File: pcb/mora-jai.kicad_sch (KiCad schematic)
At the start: 31 parts, among them J1 Conn_01x02, J2 Conn_01x04, J3 Conn_01x02, J4 Conn_01x02, J5 Conn_01x03, Q2 NPN, SW1 SW_Push, SW10 SW_Push, SW11 SW_Push, SW12 SW_Push, SW13 SW_Push, SW14 SW_Push, SW15 SW_Push, SW16 SW_Push, SW2 SW_Push, SW3 SW_Push, SW4 SW_Push, SW5 SW_Push, SW6 SW_Push, SW7 SW_Push, SW8 SW_Push, SW9 SW_Push, U1 CD74HC4067M, U3 XIAO-ESP32-S3-SMD

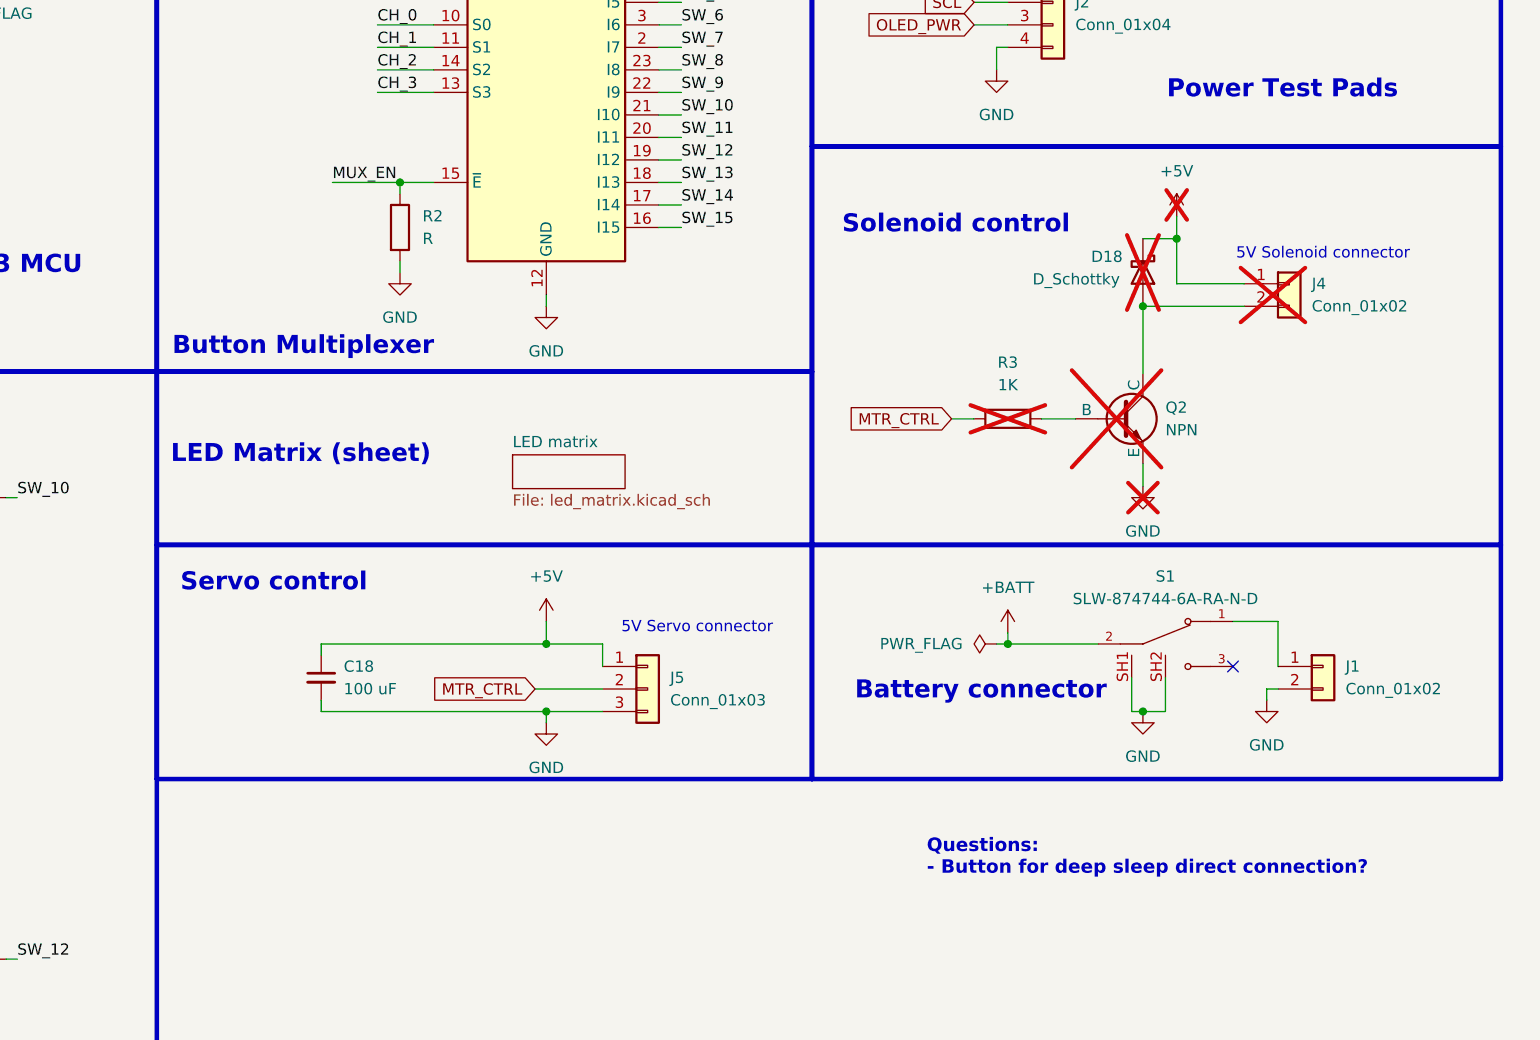
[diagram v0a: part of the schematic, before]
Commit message: remove solenoid control circuit, switching to servo
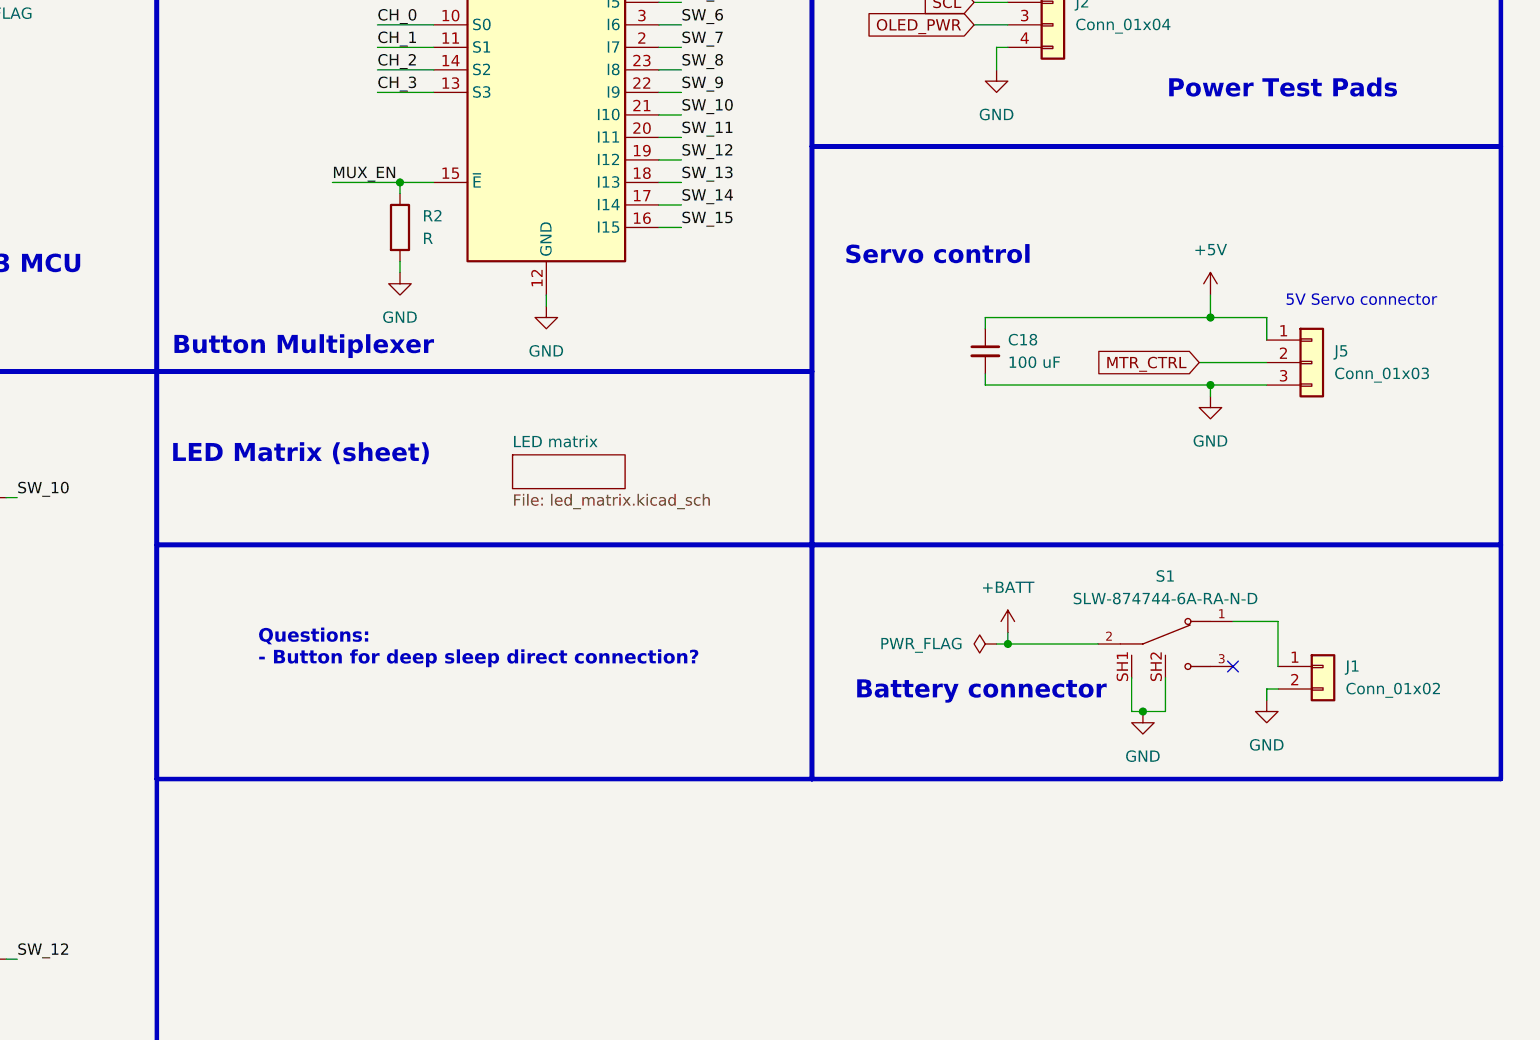
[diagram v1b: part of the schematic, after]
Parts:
- removed D18: D_Schottky, symbol Device:D_Schottky
- removed J4: Conn_01x02, Connector_JST:JST_PH_S2B-PH-K_1x02_P2.00mm_Horizontal, symbol Connector_Generic:Conn_01x02
- removed Q2: NPN, symbol Simulation_SPICE:NPN
- removed R3: 1K, symbol Device:R
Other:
- note removed: "5V Solenoid connector"
- note removed: "Solenoid control"
- moved on the sheet: C18, J5

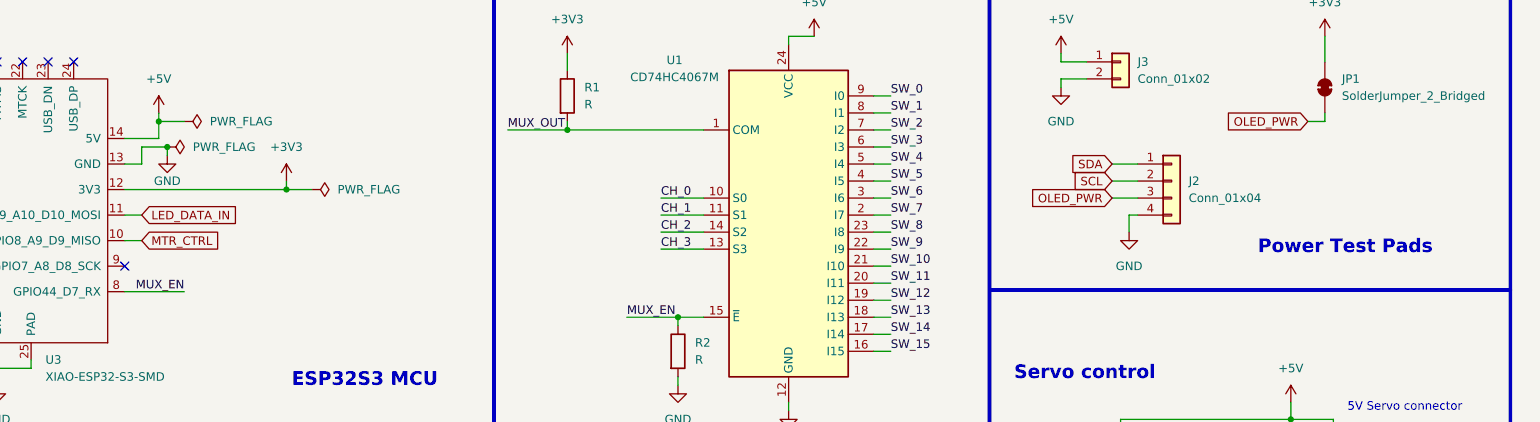
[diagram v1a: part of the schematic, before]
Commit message: positioning OLED
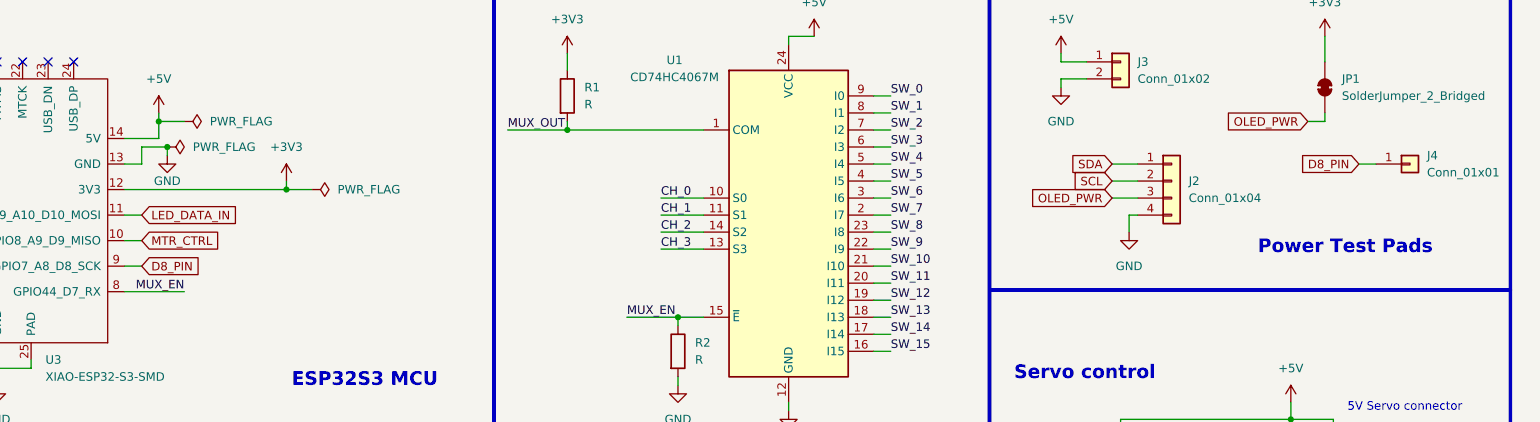
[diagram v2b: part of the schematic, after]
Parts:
- added J4: Conn_01x01, Connector_PinHeader_2.54mm:PinHeader_1x01_P2.54mm_Vertical, symbol Connector_Generic:Conn_01x01
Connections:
- net D8_PIN: now reaches U3.9 (GPIO7_A8_D8_SCK)
- net D8_PIN: now also J4.1 (Pin_1)
- no-connect marks 10 -> 9
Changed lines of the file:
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@@
 		(at 58.42 24.13)
 	)
-	(no_connect
-		(at 77.47 54.61)
-	)
 	(wire
 		(pts
@@
 	(wire
 		(pts
+			(xy 77.47 54.61) (xy 80.01 54.61)
+		)
+		(stroke
+			(width 0)
+			(type default)
+		)
+	)
+	(wire
+		(pts
 			(xy 87.63 143.51) (xy 87.63 139.7)
 		)
@@
 	(wire
 		(pts
+			(xy 261.62 39.37) (xy 264.16 39.37)
+		)
+		(stroke
+			(width 0)
+			(type default)
+		)
+	)
+	(wire
+		(pts
 			(xy 227.33 49.53) (xy 227.33 46.99)
 		)
@@
 		)
 	)
+	(global_label "D8_PIN"
+		(shape input)
+		(at 80.01 54.61 0)
+		(fields_autoplaced yes)
+		(effects
+			(font
+				(size 1.27 1.27)
+			)
+			(justify left)
+		)
+		(property "Intersheetrefs" "${INTERSHEET_REFS}"
+			(at 89.6476 54.61 0)
+			(hide yes)
+			(show_name no)
+			(do_not_autoplace no)
+			(effects
+				(font
+					(size 1.27 1.27)
+				)
+				(justify left)
+			)
+		)
+	)
+	(global_label "D8_PIN"
+		(shape input)
+		(at 261.62 39.37 180)
+		(fields_autoplaced yes)
+		(effects
+			(font
+				(size 1.27 1.27)
+			)
+			(justify right)
+		)
+		(property "Intersheetrefs" "${INTERSHEET_REFS}"
+			(at 251.9824 39.37 0)
+			(hide yes)
+			(show_name no)
+			(do_not_autoplace no)
+			(effects
+				(font
+					(size 1.27 1.27)
+				)
+				(justify right)
+			)
+		)
+	)
 	(global_label "LED_DATA_IN"
 		(shape input)
@@
 					(unit 1)
 				)
+			)
+		)
+	)
+	(symbol
+		(lib_id "Connector_Generic:Conn_01x01")
+		(at 269.24 39.37 0)
+		(unit 1)
+		(body_style 1)
+		(exclude_from_sim no)
+		(in_bom yes)
+		(on_board yes)
+		(in_pos_files yes)
+		(dnp no)
+		(fields_autoplaced yes)
+		(property "Reference" "J4"
+			(at 271.78 38.0999 0)
+			(show_name no)
+			(do_not_autoplace no)
+			(effects
+				(font
+					(size 1.27 1.27)
+				)
+				(justify left)
+			)
+		)
+		(property "Value" "Conn_01x01"
+			(at 271.78 40.6399 0)
+			(show_name no)
+			(do_not_autoplace no)
+			(effects
+				(font
+					(size 1.27 1.27)
+				)
+				(justify left)
+			)
+		)
+		(property "Footprint" "Connector_PinHeader_2.54mm:PinHeader_1x01_P2.54mm_Vertical"
+			(at 269.24 39.37 0)
+			(hide yes)
+			(show_name no)
+			(do_not_autoplace no)
+			(effects
+				(font
+					(size 1.27 1.27)
+				)
+			)
+		)
+		(property "Datasheet" ""
+			(at 269.24 39.37 0)
+			(hide yes)
+			(show_name no)
+			(do_not_autoplace no)
+			(effects
+				(font
+					(size 1.27 1.27)
+				)
+			)
+		)
+		(property "Description" "Generic connector, single row, 01x01, script generated (kicad-library-utils/schlib/autogen/connector/)"
+			(at 269.24 39.37 0)
+			(hide yes)
+			(show_name no)
+			(do_not_autoplace no)
+			(effects
+				(font
+					(size 1.27 1.27)
+				)
+			)
+		)
+		(pin "1"
+		)
+		(instances
+			(project "mora-jai"
+				(path "/06a165cb-987d-4515-950b-4b68772ab4b3"
+					(reference "J4")
+					(unit 1)
+				)

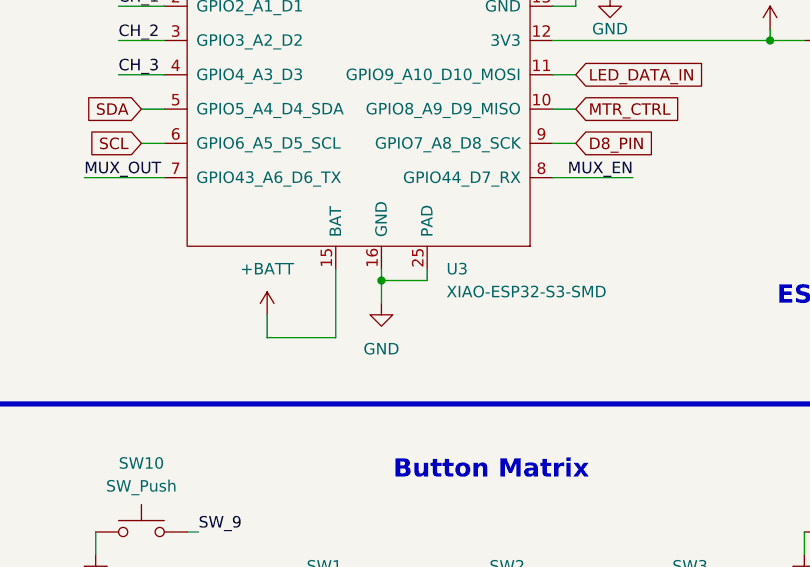
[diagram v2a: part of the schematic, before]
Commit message: begin routing LED matrix, repositioned more components
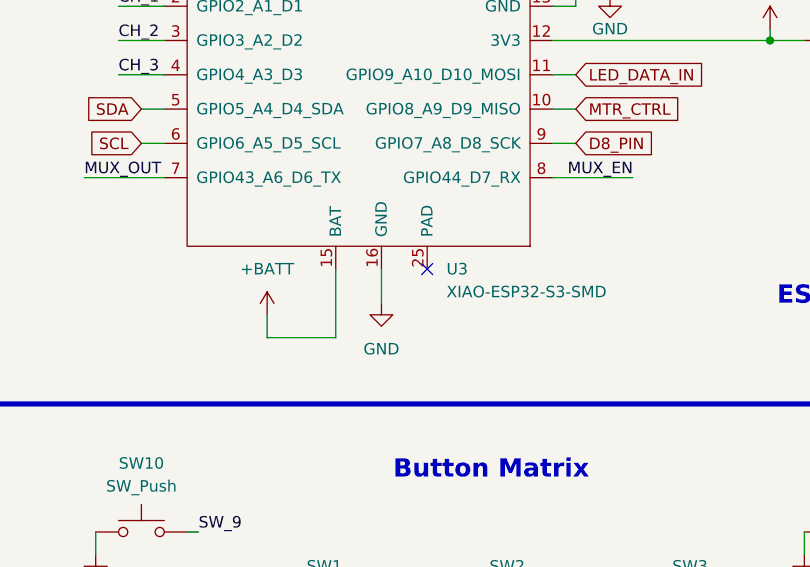
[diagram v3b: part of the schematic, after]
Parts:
- C18: footprint (none) -> Capacitor_SMD:C_0805_2012Metric_Pad1.18x1.45mm_HandSolder
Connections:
- net GND: no longer U3.25 (PAD)
- no-connect marks 9 -> 10
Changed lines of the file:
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@@
 	)
 	(junction
-		(at 58.42 69.85)
-		(diameter 0)
-		(color 0 0 0 0)
-	)
-	(junction
 		(at 46.99 124.46)
 		(diameter 0)
@@
 	)
 	(no_connect
+		(at 63.5 68.58)
+	)
+	(no_connect
 		(at 58.42 24.13)
 	)
@@
 	(wire
 		(pts
-			(xy 63.5 68.58) (xy 63.5 69.85)
-		)
-		(stroke
-			(width 0)
-			(type default)
-		)
-	)
-	(wire
-		(pts
 			(xy 67.31 113.03) (xy 67.31 109.22)
 		)
@@
 	(wire
 		(pts
-			(xy 58.42 69.85) (xy 58.42 72.39)
-		)
-		(stroke
-			(width 0)
-			(type default)
-		)
-	)
-	(wire
-		(pts
 			(xy 189.23 31.75) (xy 191.77 31.75)
 		)
@@
 	(wire
 		(pts
-			(xy 58.42 68.58) (xy 58.42 69.85)
+			(xy 58.42 68.58) (xy 58.42 72.39)
 		)
 		(stroke
@@
 	(wire
 		(pts
-			(xy 63.5 69.85) (xy 58.42 69.85)
-		)
-		(stroke
-			(width 0)
-			(type default)
-		)
-	)
-	(wire
-		(pts
 			(xy 77.47 46.99) (xy 80.01 46.99)
 		)
@@
 			)
 		)
-		(property "Footprint" ""
+		(property "Footprint" "Capacitor_SMD:C_0805_2012Metric_Pad1.18x1.45mm_HandSolder"
 			(at 226.06 81.28 0)
 			(hide yes)

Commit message: lots of routing
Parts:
- removed JP1: SolderJumper_2_Bridged, Jumper:SolderJumper-2_P1.3mm_Bridged_RoundedPad1.0x1.5mm, symbol Jumper:SolderJumper_2_Bridged
- added JP2: SolderJumper_3_Bridged12, Jumper:SolderJumper-3_P1.3mm_Bridged12_RoundedPad1.0x1.5mm, symbol Jumper:SolderJumper_3_Bridged12
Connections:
- net +3V3: now also JP2.2 (C)
- net +5V: now also JP2.3 (B)
- net OLED_PWR: now also JP2.1 (A)
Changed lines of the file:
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@@
 	(wire
 		(pts
-			(xy 256.54 31.75) (xy 256.54 33.02)
+			(xy 270.51 31.75) (xy 270.51 33.02)
 		)
 		(stroke
@@
 	(wire
 		(pts
-			(xy 256.54 20.32) (xy 256.54 24.13)
+			(xy 276.86 20.32) (xy 276.86 26.67)
+		)
+		(stroke
+			(width 0)
+			(type default)
+		)
+	)
+	(wire
+		(pts
+			(xy 270.51 20.32) (xy 270.51 21.59)
 		)
 		(stroke
@@
 	(wire
 		(pts
+			(xy 274.32 26.67) (xy 276.86 26.67)
+		)
+		(stroke
+			(width 0)
+			(type default)
+		)
+	)
+	(wire
+		(pts
 			(xy 80.01 39.37) (xy 80.01 36.83)
 		)
@@
 	(wire
 		(pts
-			(xy 256.54 33.02) (xy 254 33.02)
+			(xy 270.51 33.02) (xy 267.97 33.02)
 		)
 		(stroke
@@
 	(global_label "OLED_PWR"
 		(shape input)
-		(at 254 33.02 180)
+		(at 267.97 33.02 180)
 		(fields_autoplaced yes)
 		(effects
@@
 		)
 		(property "Intersheetrefs" "${INTERSHEET_REFS}"
-			(at 241.2782 33.02 0)
+			(at 255.2482 33.02 0)
 			(hide yes)
 			(show_name no)
@@
 	(symbol
 		(lib_id "power:+3V3")
-		(at 256.54 20.32 0)
+		(at 276.86 20.32 0)
 		(unit 1)
 		(body_style 1)
@@
 		(fields_autoplaced yes)
 		(property "Reference" "#PWR058"
-			(at 256.54 24.13 0)
+			(at 276.86 24.13 0)
 			(hide yes)
 			(show_name no)
@@
 		)
 		(property "Value" "+3V3"
-			(at 256.54 15.24 0)
+			(at 276.86 15.24 0)
 			(show_name no)
 			(do_not_autoplace no)
@@
 		)
 		(property "Footprint" ""
-			(at 256.54 20.32 0)
+			(at 276.86 20.32 0)
 			(hide yes)
 			(show_name no)
@@
 		)
 		(property "Datasheet" ""
-			(at 256.54 20.32 0)
+			(at 276.86 20.32 0)
 			(hide yes)
 			(show_name no)
@@
 		)
 		(property "Description" "Power symbol creates a global label with name \"+3V3\""
-			(at 256.54 20.32 0)
+			(at 276.86 20.32 0)
 			(hide yes)
 			(show_name no)
@@
 	)
 	(symbol
-		(lib_id "Jumper:SolderJumper_2_Bridged")
-		(at 256.54 27.94 90)
-		(unit 1)
-		(body_style 1)
-		(exclude_from_sim no)
-		(in_bom no)
-		(on_board yes)
-		(in_pos_files yes)
-		(dnp no)
-		(fields_autoplaced yes)
-		(property "Reference" "JP1"
-			(at 259.08 26.6699 90)
-			(show_name no)
-			(do_not_autoplace no)
-			(effects
-				(font
-					(size 1.27 1.27)
-				)
-				(justify right)
-			)
-		)
-		(property "Value" "SolderJumper_2_Bridged"
-			(at 259.08 29.2099 90)
-			(show_name no)
-			(do_not_autoplace no)
-			(effects
-				(font
-					(size 1.27 1.27)
-				)
-				(justify right)
-			)
-		)
-		(property "Footprint" "Jumper:SolderJumper-2_P1.3mm_Bridged_RoundedPad1.0x1.5mm"
-			(at 256.54 27.94 0)
-			(hide yes)
-			(show_name no)
-			(do_not_autoplace no)
-			(effects
-				(font
-					(size 1.27 1.27)
-				)
-			)
-		)
-		(property "Datasheet" ""
-			(at 256.54 27.94 0)
-			(hide yes)
-			(show_name no)
-			(do_not_autoplace no)
-			(effects
-				(font
-					(size 1.27 1.27)
-				)
-			)
-		)
-		(property "Description" "Solder Jumper, 2-pole, closed/bridged"
-			(at 256.54 27.94 0)
-			(hide yes)
-			(show_name no)
-			(do_not_autoplace no)
-			(effects
-				(font
-					(size 1.27 1.27)
-				)
-			)
-		)
-		(pin "2"
-		)
-		(pin "1"
-		)
-		(instances
-			(project "mora-jai"
-				(path "/06a165cb-987d-4515-950b-4b68772ab4b3"
-					(reference "JP1")
-					(unit 1)
-				)
-			)
-		)
-	)
-	(symbol
 		(lib_id "power:+BATT")
 		(at 45.72 73.66 0)
@@
 	)
 	(symbol
+		(lib_id "Jumper:SolderJumper_3_Bridged12")
+		(at 270.51 26.67 90)
+		(unit 1)
+		(body_style 1)
+		(exclude_from_sim no)
+		(in_bom no)
+		(on_board yes)
+		(in_pos_files yes)
+		(dnp no)
+		(property "Reference" "JP2"
+			(at 267.97 25.3999 90)
+			(show_name no)
+			(do_not_autoplace no)
+			(effects
+				(font
+					(size 1.27 1.27)
+				)
+				(justify left)
+			)
+		)
+		(property "Value" "SolderJumper_3_Bridged12"
+			(at 267.97 27.94 90)
+			(show_name no)
+			(do_not_autoplace no)
+			(effects
+				(font
+					(size 1.27 1.27)
+				)
+				(justify left)
+			)
+		)
+		(property "Footprint" "Jumper:SolderJumper-3_P1.3mm_Bridged12_RoundedPad1.0x1.5mm"
+			(at 270.51 26.67 0)
+			(hide yes)
+			(show_name no)
+			(do_not_autoplace no)
+			(effects
+				(font
+					(size 1.27 1.27)
+				)
+			)
+		)
+		(property "Datasheet" ""
+			(at 285.75 26.67 0)
+			(hide yes)
+			(show_name no)
+			(do_not_autoplace no)
+			(effects
+				(font
+					(size 1.27 1.27)
+				)
+			)
+		)
+		(property "Description" "3-pole Solder Jumper, pins 1+2 closed/bridged"
+			(at 283.21 26.67 0)
+			(hide yes)
+			(show_name no)
+			(do_not_autoplace no)
+			(effects
+				(font
+					(size 1.27 1.27)
+				)
+			)
+		)
+		(pin "3"
+		)
+		(pin "1"
+		)
+		(pin "2"
+		)
+		(instances
+			(project "mora-jai"
+				(path "/06a165cb-987d-4515-950b-4b68772ab4b3"
+					(reference "JP2")
+					(unit 1)
+				)
+			)
+		)
+	)
+	(symbol
 		(lib_id "Mora_Jai_Sym:SLW-874744-6A-RA-N-D")
 		(at 246.38 114.3 0)
@@
 					(unit 1)
 				)
+			)
+		)
+	)
+	(symbol
+		(lib_id "power:+5V")
+		(at 270.51 20.32 0)
+		(unit 1)
+		(body_style 1)
+		(exclude_from_sim no)
+		(in_bom yes)
+		(on_board yes)
+		(in_pos_files yes)
+		(dnp no)
+		(fields_autoplaced yes)
+		(property "Reference" "#PWR071"
+			(at 270.51 24.13 0)
+			(hide yes)
+			(show_name no)
+			(do_not_autoplace no)
+			(effects
+				(font
+					(size 1.27 1.27)
+				)
+			)
+		)
+		(property "Value" "+5V"
+			(at 270.51 15.24 0)
+			(show_name no)
+			(do_not_autoplace no)
+			(effects
+				(font
+					(size 1.27 1.27)
+				)
+			)
+		)
+		(property "Footprint" ""
+			(at 270.51 20.32 0)
+			(hide yes)
+			(show_name no)
+			(do_not_autoplace no)
+			(effects
+				(font
+					(size 1.27 1.27)
+				)
+			)
+		)
+		(property "Datasheet" ""
+			(at 270.51 20.32 0)
+			(hide yes)
+			(show_name no)
+			(do_not_autoplace no)
+			(effects
+				(font
+					(size 1.27 1.27)
+				)
+			)
+		)
+		(property "Description" "Power symbol creates a global label with name \"+5V\""
+			(at 270.51 20.32 0)
+			(hide yes)
+			(show_name no)
+			(do_not_autoplace no)
+			(effects
+				(font
+					(size 1.27 1.27)
+				)
+			)
+		)
+		(pin "1"
+		)
+		(instances
+			(project "mora-jai"
+				(path "/06a165cb-987d-4515-950b-4b68772ab4b3"
+					(reference "#PWR071")
+					(unit 1)
+				)
